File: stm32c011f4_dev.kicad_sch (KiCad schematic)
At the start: 24 parts, among them J3 Conn_01x14_Pin, J5 Conn_01x14_Pin, P1 USB_C_Plug_USB2.0, SW3 SW_Push, SW4 SW_Push, U2 STM32G030K6Tx, U3 DI78L3.3UAB-DIO, Y1 LFXTAL069528CUTT

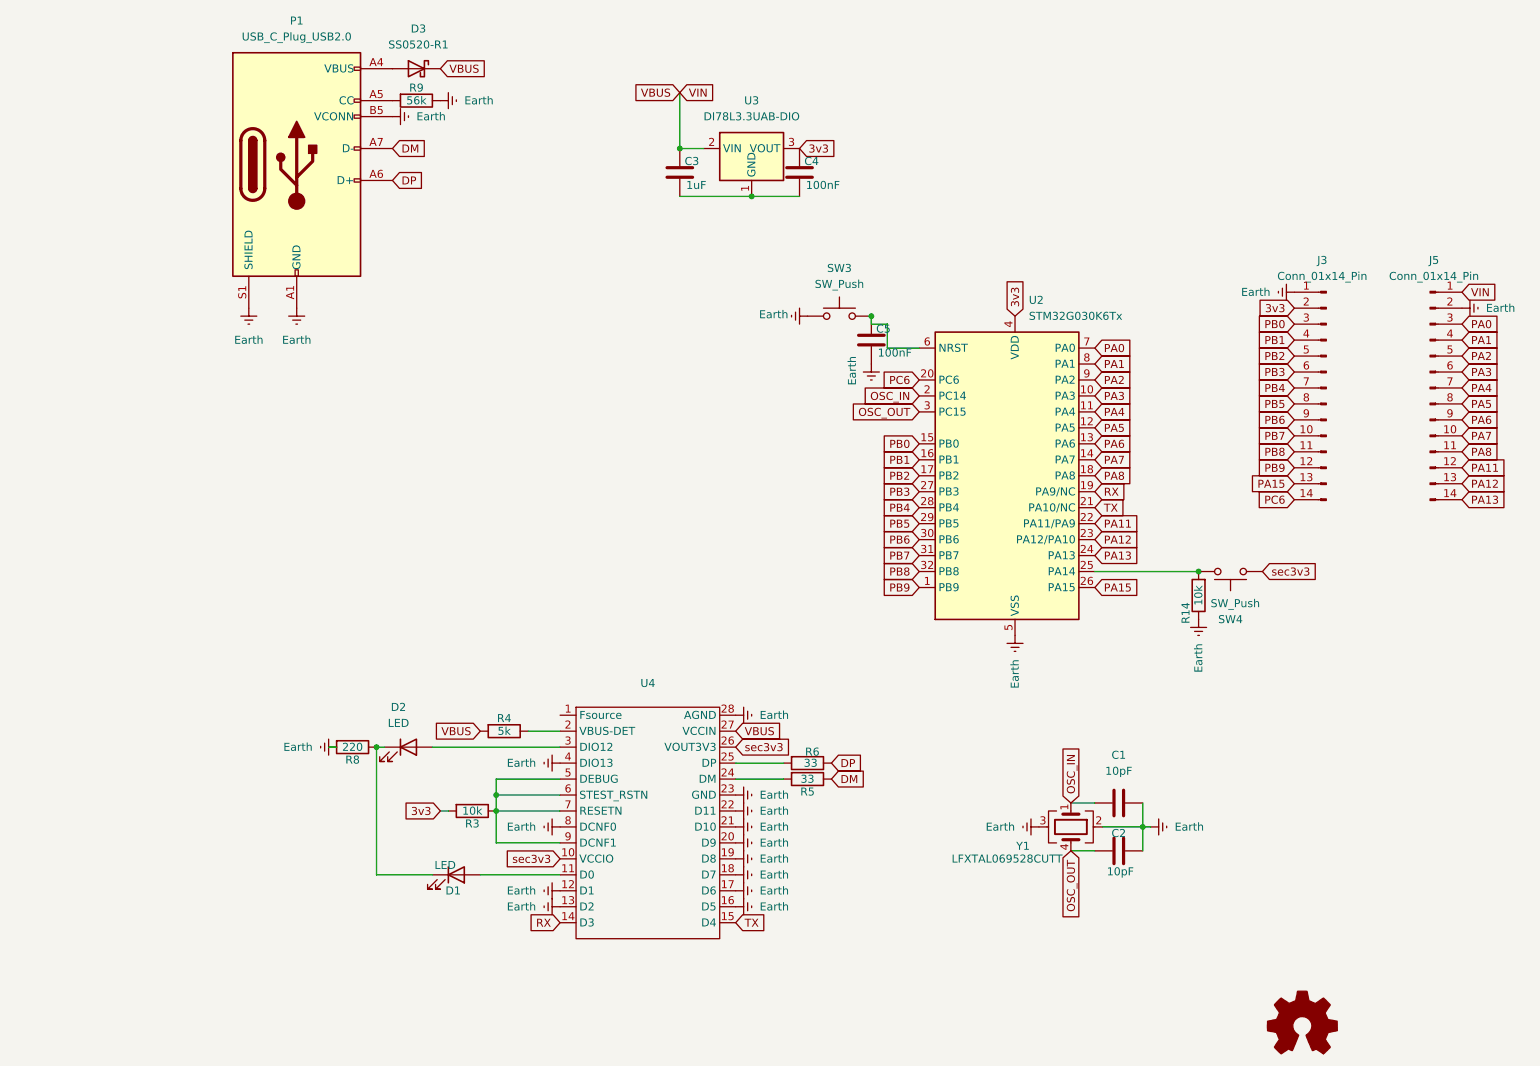
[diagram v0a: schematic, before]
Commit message: PCB update
adding swd and improving traces
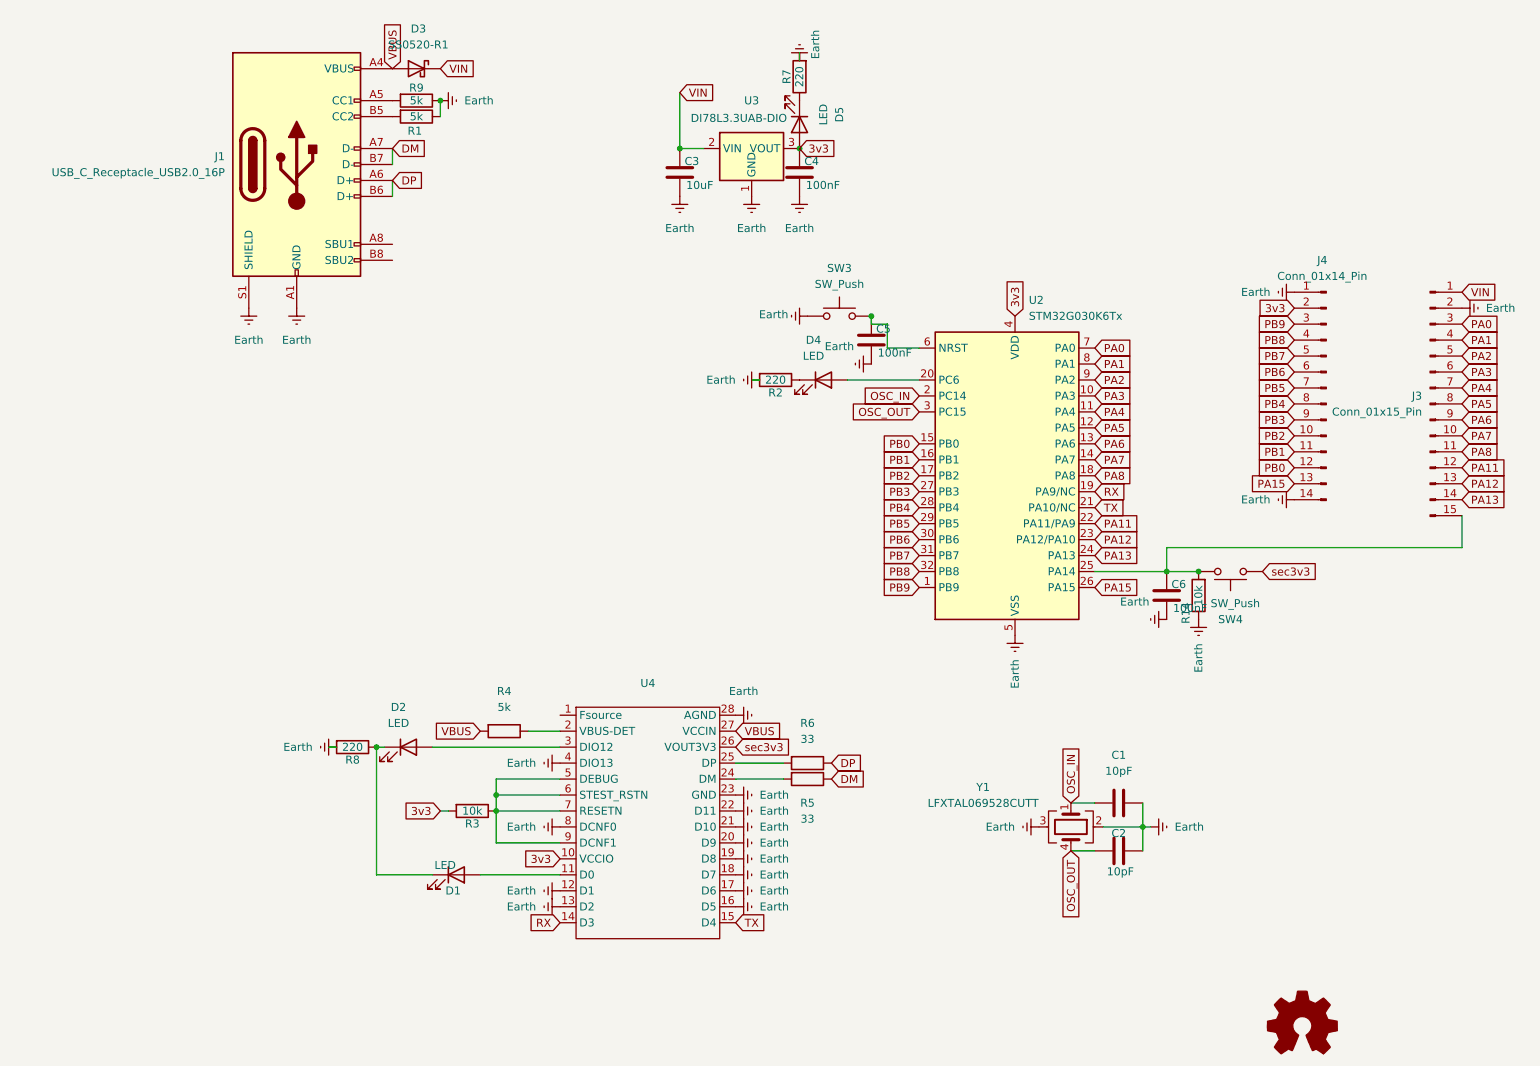
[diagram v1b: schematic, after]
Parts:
- removed J3, J5: Conn_01x14_Pin, Connector_PinHeader_2.54mm:PinHeader_1x14_P2.54mm_Vertical, symbol Connector:Conn_01x14_Pin
- removed P1: USB_C_Plug_USB2.0, Connector_USB:USB_C_Receptacle_GCT_USB4105-xx-A_16P_TopMnt_Horizontal, symbol Connector:USB_C_Plug_USB2.0
- added C6: 100nF, Capacitor_SMD:C_0603_1608Metric, symbol Device:C
- added D4, D5: LED, LED_SMD:LED_0603_1608Metric, symbol Device:LED
- added J1: USB_C_Receptacle_USB2.0_16P, Connector_USB:USB_C_Receptacle_GCT_USB4105-xx-A_16P_TopMnt_Horizontal, symbol Connector:USB_C_Receptacle_USB2.0_16P
- added J3: Conn_01x15_Pin, Connector_PinHeader_2.54mm:PinHeader_1x15_P2.54mm_Vertical, symbol Connector:Conn_01x15_Pin
- added J4: Conn_01x14_Pin, Connector_PinHeader_2.54mm:PinHeader_1x14_P2.54mm_Vertical, symbol Connector:Conn_01x14_Pin
- added R1: 5k, Resistor_SMD:R_0603_1608Metric, symbol Device:R
- added R2, R7: 220, Resistor_SMD:R_0603_1608Metric, symbol Device:R
- C3: value 1uF -> 10uF; footprint Capacitor_SMD:CP_Elec_4x5.3 -> Capacitor_SMD:C_1206_3216Metric
- R9: value 56k -> 5k
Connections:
- net 3v3: now also U4.10 (VCCIO), D5.2 (A), J4.2 (Pin_2)
- net DM: now also J1.A7 (D-), J1.B7 (D-)
- net DP: now also J1.A6 (D+), J1.B6 (D+)
- net Earth: now also C3.2, C4.2, U3.1 (GND), C6.2, J1.A1 (GND), J1.A12 (GND), J1.B1 (GND), J1.B12 (GND), J1.S1 (SHIELD), J3.2 (Pin_2), J4.1 (Pin_1), J4.14 (Pin_14), R1.1, R2.2, R7.2
- net PA0: now also J3.3 (Pin_3)
- net PA1: now also J3.4 (Pin_4)
- net PA11: now also J3.12 (Pin_12)
- net PA12: now also J3.13 (Pin_13)
- net PA13: now also J3.14 (Pin_14)
- net PA15: now also J4.13 (Pin_13)
- net PA2: now also J3.5 (Pin_5)
- net PA3: now also J3.6 (Pin_6)
- net PA4: now also J3.7 (Pin_7)
- net PA5: now also J3.8 (Pin_8)
- net PA6: now also J3.9 (Pin_9)
- net PA7: now also J3.10 (Pin_10)
- net PA8: now also J3.11 (Pin_11)
- net PB0: now also J4.12 (Pin_12)
- net PB1: now also J4.11 (Pin_11)
- net PB2: now also J4.10 (Pin_10)
- net PB3: now also J4.9 (Pin_9)
- net PB4: now also J4.8 (Pin_8)
- net PB5: now also J4.7 (Pin_7)
- net PB6: now also J4.6 (Pin_6)
- net PB7: now also J4.5 (Pin_5)
- net PB8: now also J4.4 (Pin_4)
- net PB9: now also J4.3 (Pin_3)
- net VBUS: now also D3.2 (A), J1.A4 (VBUS), J1.A9 (VBUS), J1.B4 (VBUS), J1.B9 (VBUS); no longer C3.1, D3.1 (K), U3.2 (VIN)
- net sec3v3: no longer U4.10 (VCCIO)
- net at R14.2, SW4.1, U2.25 (PA14): now also C6.1, J3.15 (Pin_15)
- net at R9.2: now also J1.A5 (CC1)
- net PC6: no longer names the net of U2.20 (PC6)
- net PC6: now also D4.2 (A)
- new net: D4.1 (K), R2.1
- new net: D5.1 (K), R7.1
- new net: J1.B5 (CC2), R1.2
- new net VIN: C3.1, D3.1 (K), J3.1 (Pin_1), U3.2 (VIN)

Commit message: Changing usb-c from smt to tht
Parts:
- removed C5: 100nF, Capacitor_SMD:C_0603_1608Metric, symbol Device:C
- removed J4: Conn_01x14_Pin, Connector_PinHeader_2.54mm:PinHeader_1x14_P2.54mm_Vertical, symbol Connector:Conn_01x14_Pin
- added J2: Conn_01x15_Pin, Connector_PinHeader_2.54mm:PinHeader_1x15_P2.54mm_Vertical, symbol Connector:Conn_01x15_Pin
- J1: footprint Connector_USB:USB_C_Receptacle_GCT_USB4105-xx-A_16P_TopMnt_Horizontal -> Connector_USB:USB_C_Receptacle_GCT_USB4085
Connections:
- net 3v3: now also J2.2 (Pin_2)
- net Earth: now also J2.1 (Pin_1), J2.14 (Pin_14)
- net PA15: now also J2.13 (Pin_13)
- net PB0: now also J2.12 (Pin_12)
- net PB1: now also J2.11 (Pin_11)
- net PB2: now also J2.10 (Pin_10)
- net PB3: now also J2.9 (Pin_9)
- net PB4: now also J2.8 (Pin_8)
- net PB5: now also J2.7 (Pin_7)
- net PB6: now also J2.6 (Pin_6)
- net PB7: now also J2.5 (Pin_5)
- net PB8: now also J2.4 (Pin_4)
- net PB9: now also J2.3 (Pin_3)
- net PC6: now reaches D4.2 (A), U2.20 (PC6)
- net PC6: now also J2.15 (Pin_15)
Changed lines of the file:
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@@
 	)
 	(junction
-		(at 116.84 60.96)
-		(diameter 0)
-		(color 0 0 0 0)
-	)
-	(junction
 		(at 57.15 139.7)
 		(diameter 0)
@@
 	(wire
 		(pts
+			(xy 163.83 97.79) (xy 210.82 97.79)
+		)
+		(stroke
+			(width 0)
+			(type default)
+		)
+	)
+	(wire
+		(pts
 			(xy 57.15 144.78) (xy 67.31 144.78)
 		)
@@
 	(wire
 		(pts
-			(xy 86.36 34.29) (xy 90.17 34.29)
+			(xy 210.82 97.79) (xy 210.82 92.71)
 		)
 		(stroke
@@
 	(wire
 		(pts
-			(xy 148.59 138.43) (xy 152.4 138.43)
+			(xy 86.36 34.29) (xy 90.17 34.29)
 		)
 		(stroke
@@
 	(wire
 		(pts
-			(xy 113.03 71.12) (xy 124.46 71.12)
+			(xy 148.59 138.43) (xy 152.4 138.43)
 		)
 		(stroke
@@
 	(wire
 		(pts
-			(xy 57.15 137.16) (xy 57.15 139.7)
+			(xy 113.03 71.12) (xy 124.46 71.12)
 		)
 		(stroke
@@
 	(wire
 		(pts
-			(xy 210.82 97.79) (xy 210.82 92.71)
+			(xy 57.15 137.16) (xy 57.15 139.7)
 		)
 		(stroke
@@
 	(wire
 		(pts
-			(xy 163.83 97.79) (xy 210.82 97.79)
-		)
-		(stroke
-			(width 0)
-			(type default)
-		)
-	)
-	(wire
-		(pts
 			(xy 38.1 149.86) (xy 38.1 129.54)
 		)
@@
 		)
 	)
+	(global_label "PC6"
+		(shape input)
+		(at 184.15 92.71 180)
+		(fields_autoplaced yes)
+		(effects
+			(font
+				(size 1.27 1.27)
+			)
+			(justify right)
+		)
+		(property "Intersheetrefs" "${INTERSHEET_REFS}"
+			(at 177.4153 92.71 0)
+			(effects
+				(font
+					(size 1.27 1.27)
+				)
+				(justify right)
+				(hide yes)
+			)
+		)
+	)
 	(global_label "3v3"
 		(shape input)
@@
 		)
 	)
+	(global_label "PC6"
+		(shape input)
+		(at 116.84 71.12 90)
+		(fields_autoplaced yes)
+		(effects
+			(font
+				(size 1.27 1.27)
+			)
+			(justify left)
+		)
+		(property "Intersheetrefs" "${INTERSHEET_REFS}"
+			(at 116.84 64.3853 90)
+			(effects
+				(font
+					(size 1.27 1.27)
+				)
+				(justify left)
+				(hide yes)
+			)
+		)
+	)
 	(global_label "PA13"
 		(shape input)
@@
 	)
 	(symbol
-		(lib_id "power:Earth")
-		(at 116.84 68.58 270)
-		(mirror x)
-		(unit 1)
-		(exclude_from_sim no)
-		(in_bom yes)
-		(on_board yes)
-		(dnp no)
-		(property "Reference" "#PWR029"
-			(at 110.49 68.58 0)
-			(effects
-				(font
-					(size 1.27 1.27)
-				)
-				(hide yes)
-			)
-		)
-		(property "Value" "Earth"
-			(at 111.76 65.786 90)
-			(effects
-				(font
-					(size 1.27 1.27)
-				)
-			)
-		)
-		(property "Footprint" ""
-			(at 116.84 68.58 0)
-			(effects
-				(font
-					(size 1.27 1.27)
-				)
-				(hide yes)
-			)
-		)
-		(property "Datasheet" "~"
-			(at 116.84 68.58 0)
-			(effects
-				(font
-					(size 1.27 1.27)
-				)
-				(hide yes)
-			)
-		)
-		(property "Description" "Power symbol creates a global label with name \"Earth\""
-			(at 116.84 68.58 0)
-			(effects
-				(font
-					(size 1.27 1.27)
-				)
-				(hide yes)
-			)
-		)
-		(pin "1"
-		)
-		(instances
-			(project "stm32c011f4_dev"
-				(path "/4e1327ae-43d4-4d8e-a3e1-cdd19cf0de2a"
-					(reference "#PWR029")
-					(unit 1)
-				)
-			)
-		)
-	)
-	(symbol
 		(lib_id "Connector:Conn_01x15_Pin")
 		(at 205.74 74.93 0)
@@
 		)
 		(property "Value" "Conn_01x15_Pin"
-			(at 204.47 76.1999 0)
+			(at 207.518 76.2 0)
 			(effects
 				(font
@@
 	)
 	(symbol
+		(lib_id "Connector:Conn_01x15_Pin")
+		(at 189.23 74.93 0)
+		(mirror y)
+		(unit 1)
+		(exclude_from_sim no)
+		(in_bom yes)
+		(on_board yes)
+		(dnp no)
+		(property "Reference" "J2"
+			(at 190.5 73.6599 0)
+			(effects
+				(font
+					(size 1.27 1.27)
+				)
+				(justify right)
+			)
+		)
+		(property "Value" "Conn_01x15_Pin"
+			(at 188.468 78.486 0)
+			(effects
+				(font
+					(size 1.27 1.27)
+				)
+				(justify right)
+			)
+		)
+		(property "Footprint" "Connector_PinHeader_2.54mm:PinHeader_1x15_P2.54mm_Vertical"
+			(at 189.23 74.93 0)
+			(effects
+				(font
+					(size 1.27 1.27)
+				)
+				(hide yes)
+			)
+		)
+		(property "Datasheet" "~"
+			(at 189.23 74.93 0)
+			(effects
+				(font
+					(size 1.27 1.27)
+				)
+				(hide yes)
+			)
+		)
+		(property "Description" "Generic connector, single row, 01x15, script generated"
+			(at 189.23 74.93 0)
+			(effects
+				(font
+					(size 1.27 1.27)
+				)
+				(hide yes)
+			)
+		)
+		(pin "4"
+		)
+		(pin "5"
+		)
+		(pin "1"
+		)
+		(pin "9"
+		)
+		(pin "2"
+		)
+		(pin "10"
+		)
+		(pin "3"
+		)
+		(pin "8"
+		)
+		(pin "14"
+		)
+		(pin "6"
+		)
+		(pin "15"
+		)
+		(pin "13"
+		)
+		(pin "7"
+		)
+		(pin "12"
+		)
+		(pin "11"
+		)
+		(instances
+			(project "stm32c011f4_dev"
+				(path "/4e1327ae-43d4-4d8e-a3e1-cdd19cf0de2a"
+					(reference "J2")
+					(unit 1)
+				)
+			)
+		)
+	)
+	(symbol
 		(lib_id "Device:LED")
 		(at 43.18 129.54 0)
@@
 			)
 		)
-		(property "Footprint" "Connector_USB:USB_C_Receptacle_GCT_USB4105-xx-A_16P_TopMnt_Horizontal"
+		(property "Footprint" "Connector_USB:USB_C_Receptacle_GCT_USB4085"
 			(at 29.21 36.83 0)
 			(effects
@@
 					(unit 1)
 				)
-			)
-		)
-	)
-	(symbol
-		(lib_id "Device:C")
-		(at 116.84 64.77 0)
-		(unit 1)
-		(exclude_from_sim no)
-		(in_bom yes)
-		(on_board yes)
-		(dnp no)
-		(property "Reference" "C5"
-			(at 117.602 62.992 0)
-			(effects
-				(font
-					(size 1.27 1.27)
-				)
-				(justify left)
-			)
-		)
-		(property "Value" "100nF"
-			(at 117.856 66.802 0)
-			(effects
-				(font
-					(size 1.27 1.27)
-				)
-				(justify left)
-			)
-		)
-		(property "Footprint" "Capacitor_SMD:C_0603_1608Metric"
-			(at 117.8052 68.58 0)
-			(effects
-				(font
-					(size 1.27 1.27)
-				)
-				(hide yes)
-			)
-		)
-		(property "Datasheet" "~"
-			(at 116.84 64.77 0)
-			(effects
-				(font
-					(size 1.27 1.27)
-				)
-				(hide yes)
-			)
-		)
-		(property "Description" "Unpolarized capacitor"
-			(at 116.84 64.77 0)
-			(effects
-				(font
-					(size 1.27 1.27)
-				)
-				(hide yes)
-			)
-		)
-		(pin "2"
-		)
-		(pin "1"
-		)
-		(instances
-			(project "stm32c011f4_dev"
-				(path "/4e1327ae-43d4-4d8e-a3e1-cdd19cf0de2a"
-					(reference "C5")
-					(unit 1)
-				)
-			)
-		)
-	)
-	(symbol
-		(lib_id "Connector:Conn_01x14_Pin")
-		(at 189.23 72.39 0)
-		(mirror y)
-		(unit 1)
-		(exclude_from_sim no)
-		(in_bom yes)
-		(on_board yes)
-		(dnp no)
-		(property "Reference" "J4"
-			(at 188.595 52.07 0)
-			(effects
-				(font
-					(size 1.27 1.27)
-				)
-			)
-		)
-		(property "Value" "Conn_01x14_Pin"
-			(at 188.595 54.61 0)
-			(effects
-				(font
-					(size 1.27 1.27)
-				)
-			)
-		)
-		(property "Footprint" "Connector_PinHeader_2.54mm:PinHeader_1x14_P2.54mm_Vertical"
-			(at 189.23 72.39 0)
-			(effects
-				(font
-					(size 1.27 1.27)
-				)
-				(hide yes)
-			)
-		)
-		(property "Datasheet" "~"
-			(at 189.23 72.39 0)
-			(effects
-				(font
-					(size 1.27 1.27)
-				)
-				(hide yes)
-			)
-		)
-		(property "Description" "Generic connector, single row, 01x14, script generated"
-			(at 189.23 72.39 0)
-			(effects
-				(font
-					(size 1.27 1.27)
-				)
-				(hide yes)
-			)
-		)
-		(pin "6"
-		)
-		(pin "1"
-		)
-		(pin "4"
-		)
-		(pin "11"
-		)
-		(pin "14"
-		)
-		(pin "2"
-		)
-		(pin "5"
-		)
-		(pin "7"
-		)
-		(pin "10"
-		)
-		(pin "9"
-		)
-		(pin "3"
-		)
-		(pin "12"
-		)
-		(pin "13"
-		)
-		(pin "8"
-		)
-		(instances
-			(project "stm32c011f4_dev"
-				(path "/4e1327ae-43d4-4d8e-a3e1-cdd19cf0de2a"
-					(reference "J4")
-					(unit 1)
-				)

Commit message: tht usb and one resistor per led cathode
:333
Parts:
- added R10: 220, Resistor_SMD:R_0603_1608Metric, symbol Device:R
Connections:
- net Earth: now also R10.2
- net at D2.1 (K), R8.1: no longer D1.1 (K)
- new net: D1.1 (K), R10.1
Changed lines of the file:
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@@
 	)
 	(junction
-		(at 38.1 129.54)
-		(diameter 0)
-		(color 0 0 0 0)
-	)
-	(junction
 		(at 86.36 34.29)
 		(diameter 0)
@@
 	(wire
 		(pts
-			(xy 38.1 149.86) (xy 38.1 129.54)
-		)
-		(stroke
-			(width 0)
-			(type default)
-		)
-	)
-	(wire
-		(pts
 			(xy 119.38 66.04) (xy 124.46 66.04)
 		)
@@
 	)
 	(symbol
+		(lib_id "power:Earth")
+		(at 30.48 149.86 270)
+		(unit 1)
+		(exclude_from_sim no)
+		(in_bom yes)
+		(on_board yes)
+		(dnp no)
+		(fields_autoplaced yes)
+		(property "Reference" "#PWR029"
+			(at 24.13 149.86 0)
+			(effects
+				(font
+					(size 1.27 1.27)
+				)
+				(hide yes)
+			)
+		)
+		(property "Value" "Earth"
+			(at 26.67 149.8599 90)
+			(effects
+				(font
+					(size 1.27 1.27)
+				)
+				(justify right)
+			)
+		)
+		(property "Footprint" ""
+			(at 30.48 149.86 0)
+			(effects
+				(font
+					(size 1.27 1.27)
+				)
+				(hide yes)
+			)
+		)
+		(property "Datasheet" "~"
+			(at 30.48 149.86 0)
+			(effects
+				(font
+					(size 1.27 1.27)
+				)
+				(hide yes)
+			)
+		)
+		(property "Description" "Power symbol creates a global label with name \"Earth\""
+			(at 30.48 149.86 0)
+			(effects
+				(font
+					(size 1.27 1.27)
+				)
+				(hide yes)
+			)
+		)
+		(pin "1"
+		)
+		(instances
+			(project "stm32c011f4_dev"
+				(path "/4e1327ae-43d4-4d8e-a3e1-cdd19cf0de2a"
+					(reference "#PWR029")
+					(unit 1)
+				)
+			)
+		)
+	)
+	(symbol
 		(lib_id "Device:C")
 		(at 156.21 138.43 90)
@@
 					(unit 1)
 				)
+			)
+		)
+	)
+	(symbol
+		(lib_id "Device:R")
+		(at 34.29 149.86 270)
+		(unit 1)
+		(exclude_from_sim no)
+		(in_bom yes)
+		(on_board yes)
+		(dnp no)
+		(property "Reference" "R10"
+			(at 34.29 151.892 90)
+			(effects
+				(font
+					(size 1.27 1.27)
+				)
+			)
+		)
+		(property "Value" "220"
+			(at 34.29 149.86 90)
+			(effects
+				(font
+					(size 1.27 1.27)
+				)
+			)
+		)
+		(property "Footprint" "Resistor_SMD:R_0603_1608Metric"
+			(at 34.29 148.082 90)
+			(effects
+				(font
+					(size 1.27 1.27)
+				)
+				(hide yes)
+			)
+		)
+		(property "Datasheet" "~"
+			(at 34.29 149.86 0)
+			(effects
+				(font
+					(size 1.27 1.27)
+				)
+				(hide yes)
+			)
+		)
+		(property "Description" "Resistor"
+			(at 34.29 149.86 0)
+			(effects
+				(font
+					(size 1.27 1.27)
+				)
+				(hide yes)
+			)
+		)
+		(pin "1"
+		)
+		(pin "2"
+		)
+		(instances
+			(project "stm32c011f4_dev"
+				(path "/4e1327ae-43d4-4d8e-a3e1-cdd19cf0de2a"
+					(reference "R10")
+					(unit 1)
+				)
